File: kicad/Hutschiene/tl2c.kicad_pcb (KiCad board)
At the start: 4 copper layers, 175.9 x 86.5 mm, 88 parts, among them IC101 ATTINY20-X, P101 12VDC, P102 RJ45, P103 CTL CONN, P104 TPI Header, P105 DRV CONN, P106 240VAC, P107 CTL PWR, P108 UG, P109 5VDC, P110 EG, P111 OG, P112 DRV PWR, P201 Mode_Bridge, P501 CONN_PIR_OG, P502 CONN_PIR_EG, P503 CONN_PIR_UG, Q301 IRLML2502, Q302 IRLML2502, Q303 IRLML2502, Q401 IRLML2502, Q402 IRLML2502, Q403 IRLML2502, SW101 TL3315NF160Q, U201 LF120ABDT-TR, U202 TPS70933

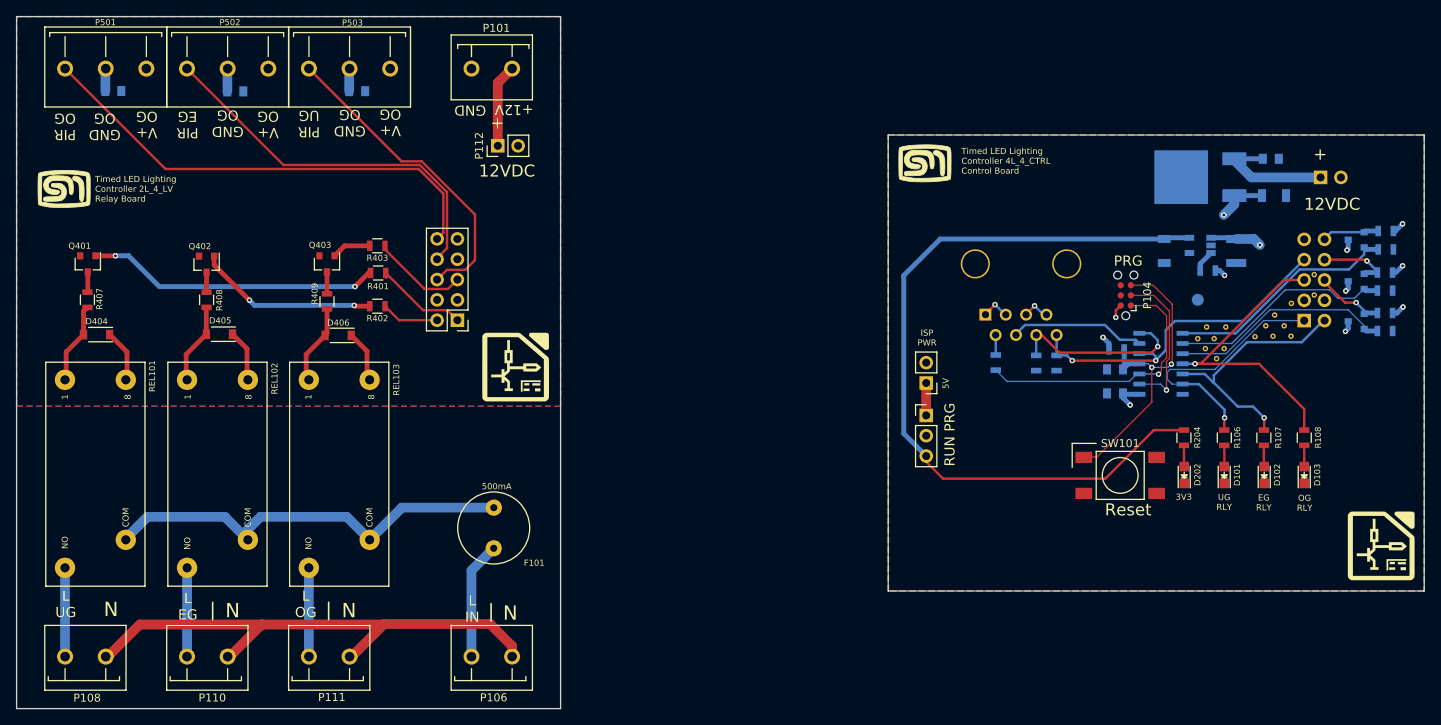
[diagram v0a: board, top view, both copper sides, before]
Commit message: More refinements based on the DIN prototype tests
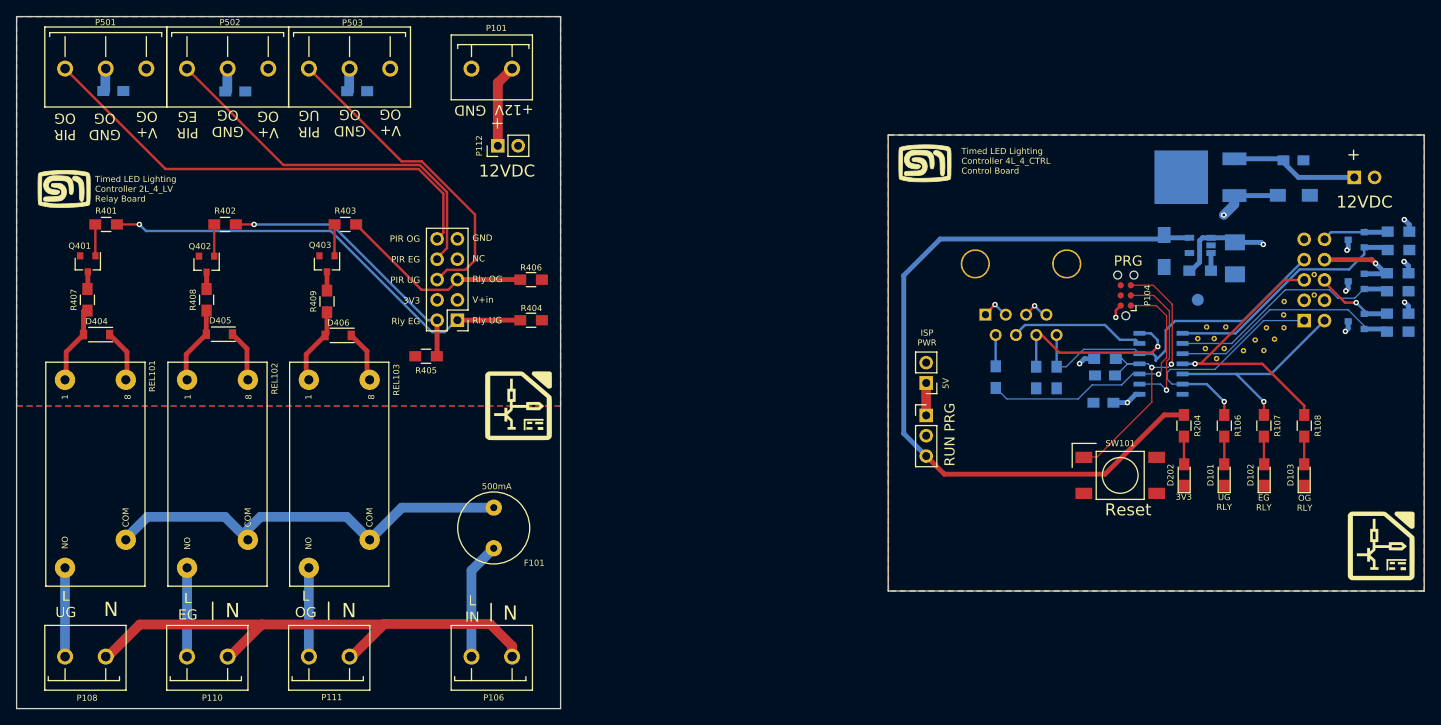
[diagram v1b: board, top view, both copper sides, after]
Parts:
- removed the REF**31 at (204.2, 98.5)
- removed the REF**31 at (201.9, 98.5)
- removed the REF**31 at (200.6, 99.8)
- removed the REF**31 at (205.1, 95.7)
- removed the REF**31 at (203.0, 97.1)
- removed the REF**31 at (205.1, 99.8)
- removed the REF**31 at (202.8, 99.8)
- added R404: 10kΩ, Resistors_SMD:R_0805_HandSoldering, F.Cu at (110.1, 97.8)
- added R405: 10kΩ, Resistors_SMD:R_0805_HandSoldering, F.Cu at (96.9, 102.3)
- added R406: 10kΩ, Resistors_SMD:R_0805_HandSoldering, F.Cu at (110.1, 92.7)
- added REF**31: Stitch_VIA, tl2c-footprint:Stitch_VIA, F.Cu at (199.1, 101.6)
- added REF**31: Stitch_VIA, tl2c-footprint:Stitch_VIA, F.Cu at (201.7, 101.5)
- added REF**31: Stitch_VIA, tl2c-footprint:Stitch_VIA, F.Cu at (200.6, 100.2)
- added REF**31: Stitch_VIA, tl2c-footprint:Stitch_VIA, F.Cu at (203.0, 100.1)
- added REF**31: Stitch_VIA, tl2c-footprint:Stitch_VIA, F.Cu at (204.2, 98.7)
- added REF**31: Stitch_VIA, tl2c-footprint:Stitch_VIA, F.Cu at (202.0, 98.7)
- added REF**31: Stitch_VIA, tl2c-footprint:Stitch_VIA, F.Cu at (204.1, 97.1)
- added REF**31: Stitch_VIA, tl2c-footprint:Stitch_VIA, F.Cu at (204.2, 95.4)
- C101, C102, C201, C501, C502, C503: footprint Capacitors_SMD:C_0805 -> Capacitors_SMD:C_0805_HandSoldering
- C202: footprint Capacitors_SMD:C_1210 -> Capacitors_SMD:C_1210_HandSoldering
- C203, C204: footprint Capacitors_SMD:C_1206 -> Capacitors_SMD:C_1206_HandSoldering
- D101, D102, D103, D202: footprint LEDs:LED_0805 -> LEDs:LED_0805_HandSoldering
- R101, R103, R104, R105, R106, R107, R108, R202, R204, R301, R302, R303, R307, R308, R309: footprint Resistors_SMD:R_0805 -> Resistors_SMD:R_0805_HandSoldering
- R401, R402, R403, R407, R408, R409: value 10kΩ -> 0kΩ; footprint Resistors_SMD:R_0805 -> Resistors_SMD:R_0805_HandSoldering
- moved R401 34.5 mm to (56.9, 85.8)
- moved R402 21.6 mm to (71.8, 85.8)
- moved G*** 4.84 mm to (108.5, 108.3)
- moved R403 4.82 mm to (86.8, 85.8)
- moved P107 4.21 mm to (213.0, 79.9)
- moved C201 2.84 mm to (205.4, 77.8)
- moved C203 2.48 mm to (205.4, 82.1)
- moved C101 1.86 mm to (181.6, 108.1)
- moved R101 1.86 mm to (181.8, 102.6)
- moved R103 1.82 mm to (168.2, 104.9)
- moved R104 1.82 mm to (173.2, 104.9)
- moved R105 1.82 mm to (175.8, 104.9)
- moved R309 1.59 mm to (218.5, 86.7)
- moved R303 1.59 mm to (218.5, 89.0)
- moved R301 1.59 mm to (218.4, 99.2)
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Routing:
- net /LED Driver/Relay_UG: track 12.0 -> 56.7 mm, vias 0 -> 1
- net Net-(Q401-Pad1): track 36.7 -> 3.92 mm, vias 2 -> 0
- net /LED Driver/Relay_EG: track 7.23 -> 34.6 mm, vias 0 -> 1
- net Net-(Q402-Pad1): track 22.7 -> 3.97 mm, vias 2 -> 0
- net /LED Driver/Relay_OG: track 12.5 -> 25.0 mm
- net /PIR13/U+: track 19.2 -> 26.5 mm, vias 6 -> 5
- net /RelayEG: track 32.1 -> 27.5 mm
- net /PIR13/PIR_EG: track 9.08 -> 11.4 mm
- net /RelayUG: track 32.7 -> 30.6 mm
- net /~Reset: track 40.1 -> 42.1 mm
- net /RelayOG: track 39.0 -> 37.3 mm
- net /SDA: track 2.51 -> 3.96 mm
- net /RLY_INT: track 22.4 -> 23.9 mm
- net /TPIDATA: track 34.0 -> 35.4 mm
- net /PIR13/PIR_OG: track 7.19 -> 8.56 mm
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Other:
- board text added: "GND NC Rly OG V+in Rly UG"
- board text added: "PIR OG PIR EG PIR UG 3V3 Rly EG"

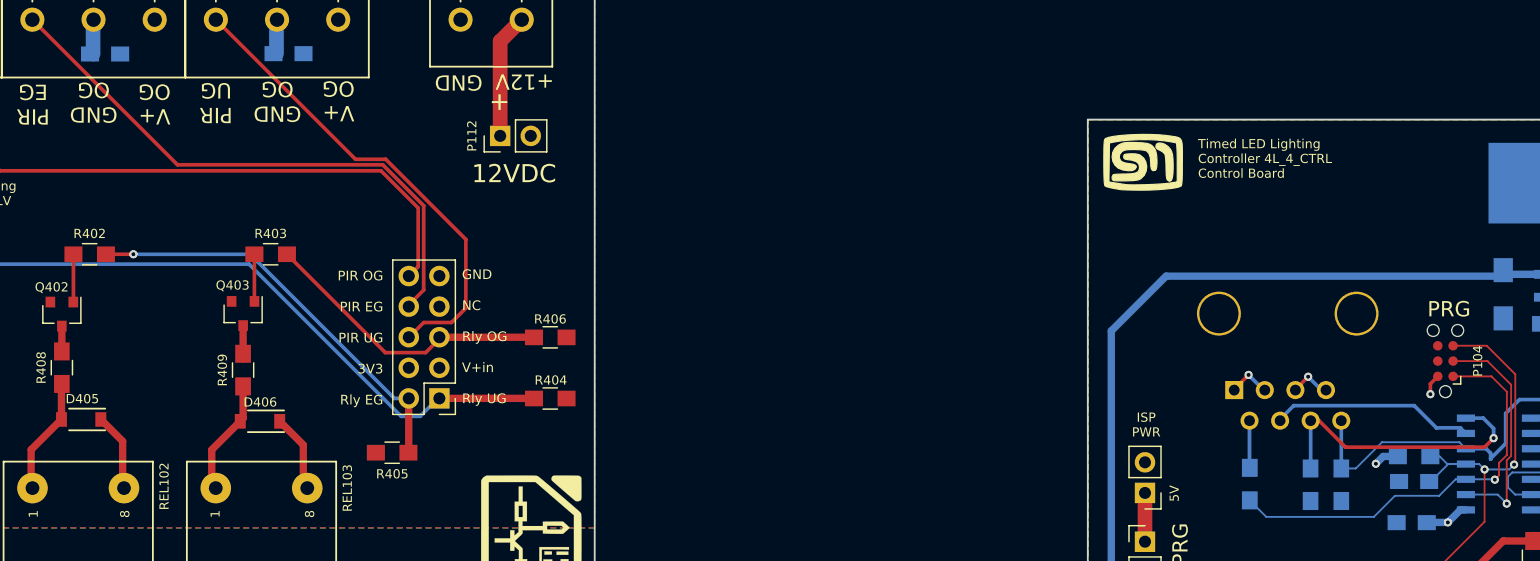
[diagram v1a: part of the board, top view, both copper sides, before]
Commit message: Enhancements to the RPi Adapter and DIN boards
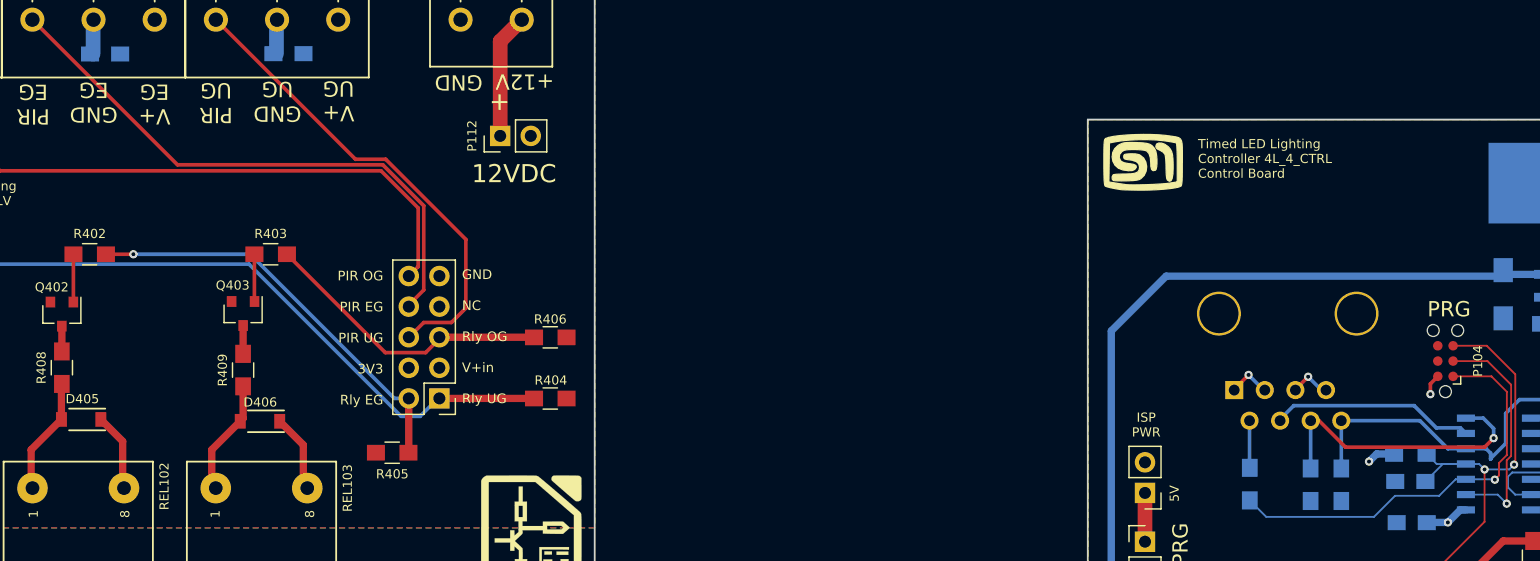
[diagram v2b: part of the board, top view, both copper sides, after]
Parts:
- moved R101 0.38 mm to (181.5, 102.4)
- moved C102 0.32 mm to (181.5, 104.6)
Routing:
- net /~Reset: track 42.1 -> 43.0 mm
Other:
- board text added: "GND EG"
- board text added: "GND UG"
- board text added: "V+ EG"
- board text added: "V+ UG"
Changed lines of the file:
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@@
     (links 160)
     (no_connects 0)
-    (area 45.674999 59.724999 221.775001 146.375001)
+    (area 20.250001 40.4 248.26 176.820001)
     (thickness 1.6)
     (drawings 107)
-    (tracks 357)
+    (tracks 354)
     (zones 0)
     (modules 92)
@@
   )
   (module Capacitors_SMD:C_0805_HandSoldering (layer B.Cu)
-    (at 181.8 104.65 180)
+    (at 181.483 104.648 180)
     (descr "Capacitor SMD 0805, hand soldering")
     (tags "capacitor 0805")
@@
   )
   (module Resistors_SMD:R_0805_HandSoldering (layer B.Cu)
-    (at 181.8 102.57 180)
+    (at 181.483 102.362 180)
     (descr "Resistor SMD 0805, hand soldering")
     (tags "resistor 0805")
@@
     (effects (font (size 1.27 1.27) (thickness 0.1778)))
   )
-  (gr_text "GND\nOG" (at 72.14 73.15 180) (layer F.SilkS)
+  (gr_text "GND\nEG" (at 72.14 73.15 180) (layer F.SilkS)
     (effects (font (size 1.27 1.27) (thickness 0.1778)))
   )
-  (gr_text "GND\nOG" (at 87.4 73.08 180) (layer F.SilkS)
+  (gr_text "GND\nUG" (at 87.4 73.08 180) (layer F.SilkS)
     (effects (font (size 1.27 1.27) (thickness 0.1778)))
   )
-  (gr_text "V+\nOG" (at 92.47 73.04 180) (layer F.SilkS)
+  (gr_text "V+\nUG" (at 92.47 73.04 180) (layer F.SilkS)
     (effects (font (size 1.27 1.27) (thickness 0.1778)))
   )
-  (gr_text "V+\nOG" (at 77.19 73.3 180) (layer F.SilkS)
+  (gr_text "V+\nEG" (at 77.19 73.3 180) (layer F.SilkS)
     (effects (font (size 1.27 1.27) (thickness 0.1778)))
   )
@@
   (segment (start 191.67 112.29) (end 191.67 115.72) (width 0.3048) (layer F.Cu) (net 33))
   (segment (start 191.67 115.72) (end 191.7 115.75) (width 0.3048) (layer F.Cu) (net 33))
+  (segment (start 182.733 104.648) (end 184.181 103.2) (width 0.1524) (layer B.Cu) (net 34) (status 400000))
+  (segment (start 184.181 103.2) (end 186.1 103.2) (width 0.1524) (layer B.Cu) (net 34) (status 800000))
+  (segment (start 182.833 102.362) (end 183.671 103.2) (width 0.1524) (layer B.Cu) (net 34) (status 400000))
+  (segment (start 183.671 103.2) (end 186.1 103.2) (width 0.1524) (layer B.Cu) (net 34) (status 800000))
   (segment (start 183.05 104.65) (end 183.19 104.65) (width 0.1524) (layer B.Cu) (net 34))
-  (segment (start 183.19 104.65) (end 184.64 103.2) (width 0.1524) (layer B.Cu) (net 34))
-  (segment (start 184.64 103.2) (end 186.1 103.2) (width 0.1524) (layer B.Cu) (net 34))
   (segment (start 182.85 105.07) (end 182.85 104.84) (width 0.1524) (layer B.Cu) (net 34))
-  (segment (start 183.15 102.57) (end 183.92 102.57) (width 0.1524) (layer B.Cu) (net 34))
-  (segment (start 184.55 103.2) (end 186.1 103.2) (width 0.1524) (layer B.Cu) (net 34))
-  (segment (start 183.92 102.57) (end 184.55 103.2) (width 0.1524) (layer B.Cu) (net 34))
   (segment (start 185.035 93.38) (end 187.83 93.38) (width 0.1524) (layer F.Cu) (net 34))
   (segment (start 189.7 103.65) (end 187.65 103.65) (width 0.1524) (layer B.Cu) (net 34))
@@
   (segment (start 104.94 135.73) (end 91.69 135.73) (width 1.2192) (layer F.Cu) (net 39))
   (segment (start 107.69 138.48) (end 104.94 135.73) (width 1.2192) (layer F.Cu) (net 39))
-  (segment (start 175.75 103.57) (end 176.95 103.57) (width 0.1524) (layer B.Cu) (net 40))
-  (segment (start 185.56 101.39) (end 186.1 101.93) (width 0.1524) (layer B.Cu) (net 40))
-  (segment (start 179.13 101.39) (end 185.56 101.39) (width 0.1524) (layer B.Cu) (net 40))
-  (segment (start 176.95 103.57) (end 179.13 101.39) (width 0.1524) (layer B.Cu) (net 40))
+  (segment (start 175.75 99.6) (end 182.277 99.6) (width 0.3048) (layer B.Cu) (net 40))
+  (segment (start 184.607 101.93) (end 186.1 101.93) (width 0.3048) (layer B.Cu) (net 40))
+  (segment (start 182.277 99.6) (end 184.607 101.93) (width 0.3048) (layer B.Cu) (net 40))
   (segment (start 175.75 99.6) (end 175.75 103.57) (width 0.3048) (layer B.Cu) (net 40))
   (segment (start 188.15 102.8) (end 188.15 102.75) (width 0.3048) (layer B.Cu) (net 40))
-  (segment (start 188.15 102.8) (end 188.15 102.3) (width 0.3048) (layer B.Cu) (net 40))
-  (segment (start 188.15 102.3) (end 187.78 101.93) (width 0.3048) (layer B.Cu) (net 40))
-  (segment (start 187.78 101.93) (end 186.1 101.93) (width 0.3048) (layer B.Cu) (net 40))
-  (segment (start 188.15 102.75) (end 189.4 101.5) (width 0.3048) (layer B.Cu) (net 40))
-  (segment (start 189.4 101.5) (end 189.4 99) (width 0.3048) (layer B.Cu) (net 40))
-  (segment (start 189.4 99) (end 190.55 97.85) (width 0.3048) (layer B.Cu) (net 40))
-  (segment (start 190.55 97.85) (end 199.03 97.85) (width 0.3048) (layer B.Cu) (net 40))
   (segment (start 199.03 97.85) (end 206.7 90.18) (width 0.3048) (layer B.Cu) (net 40))
+  (segment (start 190.55 97.85) (end 199.03 97.85) (width 0.3048) (layer B.Cu) (net 40))
+  (segment (start 189.4 99) (end 190.55 97.85) (width 0.3048) (layer B.Cu) (net 40))
+  (segment (start 189.4 101.5) (end 189.4 99) (width 0.3048) (layer B.Cu) (net 40))
+  (segment (start 188.15 102.75) (end 189.4 101.5) (width 0.3048) (layer B.Cu) (net 40))
+  (segment (start 187.78 101.93) (end 186.1 101.93) (width 0.3048) (layer B.Cu) (net 40))
+  (segment (start 188.15 102.3) (end 187.78 101.93) (width 0.3048) (layer B.Cu) (net 40))
+  (segment (start 188.15 102.8) (end 188.15 102.3) (width 0.3048) (layer B.Cu) (net 40))
   (segment (start 186.55 101.93) (end 186.1 101.93) (width 0.1524) (layer B.Cu) (net 40))
   (segment (start 159.45 105.6) (end 159.45 109.65) (width 1.2192) (layer F.Cu) (net 41))
@@
   (segment (start 188.47 104.47) (end 186.1 104.47) (width 0.1524) (layer B.Cu) (net 44))
   (segment (start 186.1 104.47) (end 185.765198 104.47) (width 0.1524) (layer B.Cu) (net 44))
+  (segment (start 180.133 102.362) (end 178.689 102.362) (width 0.6096) (layer B.Cu) (net 45) (status 400000))
+  (via (at 178.054 102.997) (size 0.6858) (drill 0.3302) (layers F.Cu B.Cu) (net 45))
+  (segment (start 178.689 102.362) (end 178.054 102.997) (width 0.6096) (layer B.Cu) (net 45))
   (segment (start 182.87 108.05) (end 184.6 108.05) (width 0.6096) (layer B.Cu) (net 45))
   (via (at 184.6 108.05) (size 0.6858) (drill 0.3302) (layers F.Cu B.Cu) (net 45))
@@
   (segment (start 182.87 108.05) (end 182.85 108.07) (width 0.6096) (layer B.Cu) (net 45))
   (segment (start 186.1 107.01) (end 185.64 107.01) (width 0.6096) (layer B.Cu) (net 45))
-  (segment (start 180.45 102.57) (end 179.23 102.57) (width 0.6096) (layer B.Cu) (net 45))
-  (segment (start 178.62 103.18) (end 178.62 103.15) (width 0.6096) (layer F.Cu) (net 45))
-  (via (at 178.62 103.18) (size 0.6858) (drill 0.3302) (layers F.Cu B.Cu) (net 45))
-  (segment (start 179.23 102.57) (end 178.62 103.18) (width 0.6096) (layer B.Cu) (net 45))
   (segment (start 183.765 95.92) (end 183.15 96.535) (width 0.3048) (layer F.Cu) (net 45))
   (via (at 183.15 97.4) (size 0.6858) (drill 0.3302) (layers F.Cu B.Cu) (net 45))
